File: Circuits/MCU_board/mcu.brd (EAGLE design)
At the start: 100 x 80 mm, 33 parts, among them U1 TCA9548APWR, U2 USBLC6-2P6, U3 LD39050PU33R, U4 LSM9DS1, U5 STM32L452RECT6

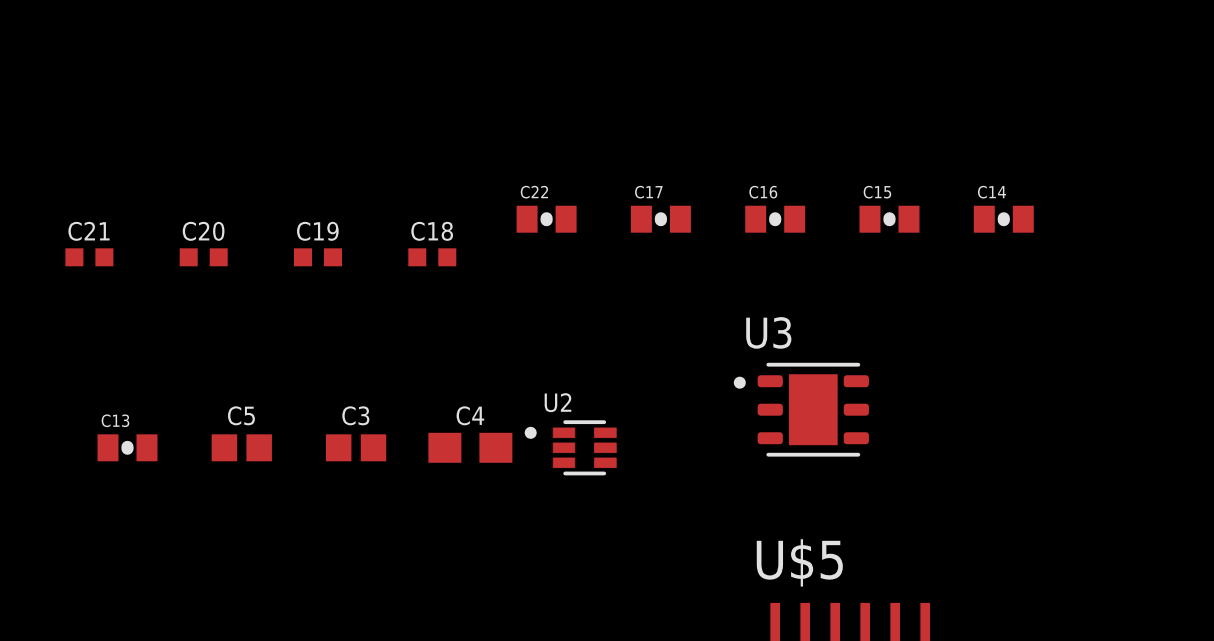
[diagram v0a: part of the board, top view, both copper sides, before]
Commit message: Delete caps
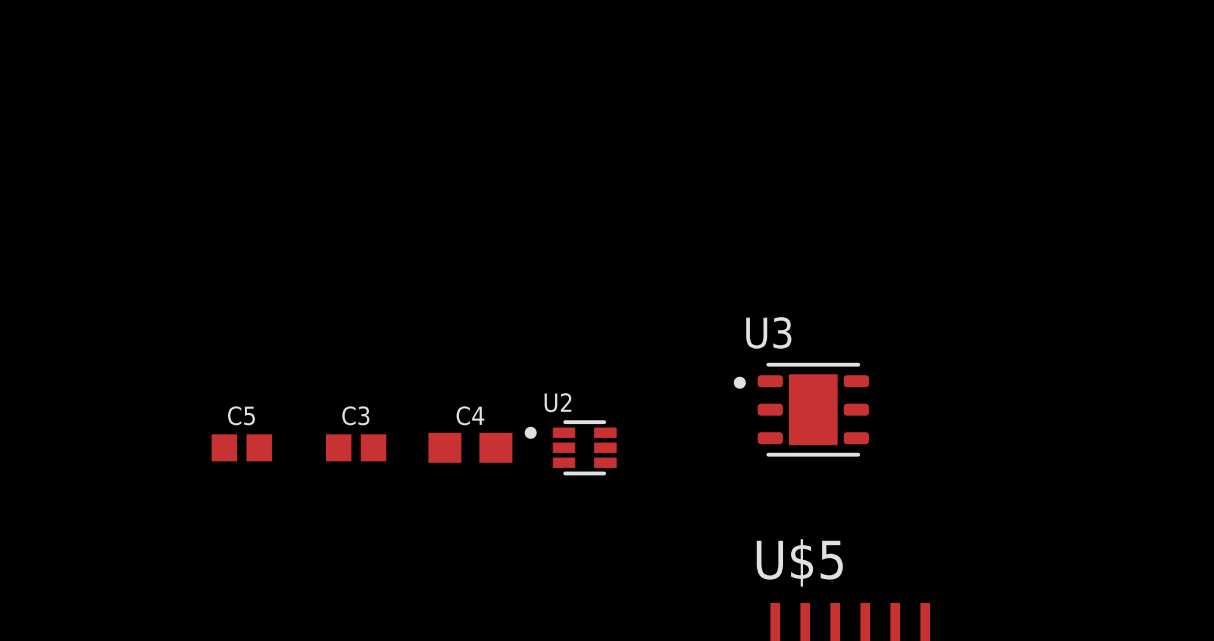
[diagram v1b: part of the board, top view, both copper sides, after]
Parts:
- removed C13, C14, C15, C16, C17, C22: 0.1uF, SparkFun-Retired:0402-CAP
- removed C18, C19, C20, C21: 2.2uF, SparkFun-Capacitors:0402-TIGHT
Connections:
- removed net N$21: C15.1, U5.48
- removed net N$22: C19.1, U5.47
- removed net N$26: C21.1, U5.18
- removed net N$29: C17.1, U5.64
- removed net N$30: C18.1, U5.63
- removed net N$31: C22.1, U5.31
- new net VDDA/VREF+: U5.13
- new net VDDUSB: U5.48
- new net VSS: U5.18, U5.31, U5.47, U5.63
- new net VSSA/VREF-: U5.12
- net GND: no longer C13.2, C14.2, C15.2, C16.2, C17.2, C18.2, C19.2, C20.2, C21.2, C22.2
- net VDD: now also U5.64; no longer C13.1, C14.1, C16.1, C20.1, U5.12, U5.13

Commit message: asdf
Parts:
- added C10, C12, C14, C16: 4.7uF, SparkFun-Capacitors:0603
- added C11, C13, C15, C9: 100nF, SparkFun-Capacitors:0603
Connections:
- removed net VDDUSB: U5.48
- removed net VSS: U5.18, U5.31, U5.47, U5.63
- net GND: now also C10.2, C11.2, C12.2, C13.2, C14.2, C15.2, C16.2, C9.2, U5.18, U5.31, U5.47, U5.63
- net VDD: now also C10.1, C11.1, C12.1, C13.1, C14.1, C15.1, C16.1, C9.1, U5.48
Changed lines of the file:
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@@
 <attribute name="VALUE" x="-44.45" y="-13.462" size="0.6096" layer="27" font="vector" ratio="20" align="top-center"/>
+</element>
+<element name="C9" library="SparkFun-Capacitors" package="0603" value="100nF" x="-44.45" y="-20.32" smashed="yes">
+<attribute name="NAME" x="-44.45" y="-19.558" size="0.6096" layer="25" font="vector" ratio="20" align="bottom-center"/>
+<attribute name="PROD_ID" value="CAP-12380" x="-44.45" y="-20.32" size="1.778" layer="27" display="off"/>
+<attribute name="VALUE" x="-44.45" y="-21.082" size="0.6096" layer="27" font="vector" ratio="20" align="top-center"/>
+</element>
+<element name="C10" library="SparkFun-Capacitors" package="0603" value="4.7uF" x="-44.45" y="-24.13" smashed="yes">
+<attribute name="NAME" x="-44.45" y="-23.368" size="0.6096" layer="25" font="vector" ratio="20" align="bottom-center"/>
+<attribute name="PROD_ID" value="CAP-12380" x="-44.45" y="-24.13" size="1.778" layer="27" display="off"/>
+<attribute name="VALUE" x="-44.45" y="-24.892" size="0.6096" layer="27" font="vector" ratio="20" align="top-center"/>
+</element>
+<element name="C11" library="SparkFun-Capacitors" package="0603" value="100nF" x="-44.45" y="-27.94" smashed="yes">
+<attribute name="NAME" x="-44.45" y="-27.178" size="0.6096" layer="25" font="vector" ratio="20" align="bottom-center"/>
+<attribute name="PROD_ID" value="CAP-12380" x="-44.45" y="-27.94" size="1.778" layer="27" display="off"/>
+<attribute name="VALUE" x="-44.45" y="-28.702" size="0.6096" layer="27" font="vector" ratio="20" align="top-center"/>
+</element>
+<element name="C12" library="SparkFun-Capacitors" package="0603" value="4.7uF" x="-44.45" y="-31.75" smashed="yes">
+<attribute name="NAME" x="-44.45" y="-30.988" size="0.6096" layer="25" font="vector" ratio="20" align="bottom-center"/>
+<attribute name="PROD_ID" value="CAP-12380" x="-44.45" y="-31.75" size="1.778" layer="27" display="off"/>
+<attribute name="VALUE" x="-44.45" y="-32.512" size="0.6096" layer="27" font="vector" ratio="20" align="top-center"/>
+</element>
+<element name="C13" library="SparkFun-Capacitors" package="0603" value="100nF" x="-44.45" y="-35.56" smashed="yes">
+<attribute name="NAME" x="-44.45" y="-34.798" size="0.6096" layer="25" font="vector" ratio="20" align="bottom-center"/>
+<attribute name="PROD_ID" value="CAP-12380" x="-44.45" y="-35.56" size="1.778" layer="27" display="off"/>
+<attribute name="VALUE" x="-44.45" y="-36.322" size="0.6096" layer="27" font="vector" ratio="20" align="top-center"/>
+</element>
+<element name="C14" library="SparkFun-Capacitors" package="0603" value="4.7uF" x="-44.45" y="-39.37" smashed="yes">
+<attribute name="NAME" x="-44.45" y="-38.608" size="0.6096" layer="25" font="vector" ratio="20" align="bottom-center"/>
+<attribute name="PROD_ID" value="CAP-12380" x="-44.45" y="-39.37" size="1.778" layer="27" display="off"/>
+<attribute name="VALUE" x="-44.45" y="-40.132" size="0.6096" layer="27" font="vector" ratio="20" align="top-center"/>
+</element>
+<element name="C15" library="SparkFun-Capacitors" package="0603" value="100nF" x="-44.45" y="-43.18" smashed="yes">
+<attribute name="NAME" x="-44.45" y="-42.418" size="0.6096" layer="25" font="vector" ratio="20" align="bottom-center"/>
+<attribute name="PROD_ID" value="CAP-12380" x="-44.45" y="-43.18" size="1.778" layer="27" display="off"/>
+<attribute name="VALUE" x="-44.45" y="-43.942" size="0.6096" layer="27" font="vector" ratio="20" align="top-center"/>
+</element>
+<element name="C16" library="SparkFun-Capacitors" package="0603" value="4.7uF" x="-44.45" y="-46.99" smashed="yes">
+<attribute name="NAME" x="-44.45" y="-46.228" size="0.6096" layer="25" font="vector" ratio="20" align="bottom-center"/>
+<attribute name="PROD_ID" value="CAP-12380" x="-44.45" y="-46.99" size="1.778" layer="27" display="off"/>
+<attribute name="VALUE" x="-44.45" y="-47.752" size="0.6096" layer="27" font="vector" ratio="20" align="top-center"/>
 </element>
 </elements>
@@
 <contactref element="U4" pad="20"/>
 <contactref element="U4" pad="19"/>
+<contactref element="C9" pad="2"/>
+<contactref element="C10" pad="2"/>
+<contactref element="C11" pad="2"/>
+<contactref element="C12" pad="2"/>
+<contactref element="C13" pad="2"/>
+<contactref element="C14" pad="2"/>
+<contactref element="C15" pad="2"/>
+<contactref element="C16" pad="2"/>
+<contactref element="U5" pad="63"/>
+<contactref element="U5" pad="47"/>
+<contactref element="U5" pad="31"/>
+<contactref element="U5" pad="18"/>
 <wire x1="32.635" y1="51.6922" x2="39.135" y2="51.6922" width="0" layer="19" extent="1-1"/>
 <wire x1="31.985" y1="51.6922" x2="32.635" y2="51.6922" width="0" layer="19" extent="1-1"/>
@@
 <wire x1="-20.86" y1="27.87" x2="-20.86" y2="36.76" width="0" layer="19" extent="1-1"/>
 <wire x1="-20.86" y1="18.98" x2="-20.86" y2="27.87" width="0" layer="19" extent="1-1"/>
-<wire x1="-34.83" y1="18.98" x2="-20.86" y2="18.98" width="0" layer="19" extent="1-1"/>
+<wire x1="-23.57" y1="13.37" x2="-20.86" y2="18.98" width="0" layer="19" extent="1-1"/>
+<wire x1="-31.42" y1="9.144" x2="-23.57" y2="13.37" width="0" layer="19" extent="1-1"/>
+<wire x1="-32.22" y1="9.144" x2="-31.42" y2="9.144" width="0" layer="19" extent="1-1"/>
+<wire x1="-14.57" y1="10.87" x2="-23.57" y2="13.37" width="0" layer="19" extent="1-1"/>
+<wire x1="-17.07" y1="1.87" x2="-14.57" y2="10.87" width="0" layer="19" extent="1-1"/>
+<wire x1="-23.57" y1="1.87" x2="-17.07" y2="1.87" width="0" layer="19" extent="1-1"/>
+<wire x1="-34.83" y1="18.98" x2="-32.22" y2="9.144" width="0" layer="19" extent="1-1"/>
 <wire x1="-34.83" y1="27.87" x2="-34.83" y2="18.98" width="0" layer="19" extent="1-1"/>
-<wire x1="-32.22" y1="9.144" x2="-34.83" y2="18.98" width="0" layer="19" extent="1-1"/>
-<wire x1="-31.42" y1="9.144" x2="-32.22" y2="9.144" width="0" layer="19" extent="1-1"/>
 <wire x1="-35.98" y1="-2.54" x2="-32.22" y2="9.144" width="0" layer="19" extent="1-1"/>
 <wire x1="-39.79" y1="-2.54" x2="-35.98" y2="-2.54" width="0" layer="19" extent="1-1"/>
@@
 <wire x1="-39.79" y1="-8.89" x2="-43.6" y2="-8.89" width="0" layer="19" extent="1-1"/>
 <wire x1="-35.98" y1="-8.89" x2="-39.79" y2="-8.89" width="0" layer="19" extent="1-1"/>
+<wire x1="-43.6" y1="-20.32" x2="-43.6" y2="-8.89" width="0" layer="19" extent="1-1"/>
+<wire x1="-43.6" y1="-24.13" x2="-43.6" y2="-20.32" width="0" layer="19" extent="1-1"/>
+<wire x1="-43.6" y1="-27.94" x2="-43.6" y2="-24.13" width="0" layer="19" extent="1-1"/>
+<wire x1="-43.6" y1="-31.75" x2="-43.6" y2="-27.94" width="0" layer="19" extent="1-1"/>
+<wire x1="-43.6" y1="-35.56" x2="-43.6" y2="-31.75" width="0" layer="19" extent="1-1"/>
+<wire x1="-43.6" y1="-39.37" x2="-43.6" y2="-35.56" width="0" layer="19" extent="1-1"/>
+<wire x1="-43.6" y1="-43.18" x2="-43.6" y2="-39.37" width="0" layer="19" extent="1-1"/>
+<wire x1="-43.6" y1="-46.99" x2="-43.6" y2="-43.18" width="0" layer="19" extent="1-1"/>
 </signal>
 <signal name="SWDIO">
@@
 <contactref element="U3" pad="4"/>
 <contactref element="C3" pad="1"/>
+<contactref element="C10" pad="1"/>
+<contactref element="C9" pad="1"/>
+<contactref element="C12" pad="1"/>
+<contactref element="C11" pad="1"/>
+<contactref element="C14" pad="1"/>
+<contactref element="C13" pad="1"/>
+<contactref element="C16" pad="1"/>
+<contactref element="C15" pad="1"/>
 <contactref element="U5" pad="64"/>
+<contactref element="U5" pad="48"/>
+<contactref element="U5" pad="32"/>
 <contactref element="U5" pad="19"/>
-<contactref element="U5" pad="32"/>
-<wire x1="-20.155" y1="43.5" x2="31.985" y2="57.5278" width="0" layer="19" extent="1-1"/>
+<wire x1="-45.3" y1="-43.18" x2="-45.3" y2="-46.99" width="0" layer="19" extent="1-1"/>
+<wire x1="-45.3" y1="-39.37" x2="-45.3" y2="-43.18" width="0" layer="19" extent="1-1"/>
+<wire x1="-45.3" y1="-35.56" x2="-45.3" y2="-39.37" width="0" layer="19" extent="1-1"/>
+<wire x1="-45.3" y1="-31.75" x2="-45.3" y2="-35.56" width="0" layer="19" extent="1-1"/>
+<wire x1="-45.3" y1="-27.94" x2="-45.3" y2="-31.75" width="0" layer="19" extent="1-1"/>
+<wire x1="-45.3" y1="-24.13" x2="-45.3" y2="-27.94" width="0" layer="19" extent="1-1"/>
+<wire x1="-45.3" y1="-20.32" x2="-45.3" y2="-24.13" width="0" layer="19" extent="1-1"/>
+<wire x1="-23.07" y1="1.87" x2="-45.3" y2="-20.32" width="0" layer="19" extent="1-1"/>
+<wire x1="-16.57" y1="1.87" x2="-23.07" y2="1.87" width="0" layer="19" extent="1-1"/>
+<wire x1="-14.57" y1="11.37" x2="-16.57" y2="1.87" width="0" layer="19" extent="1-1"/>
+<wire x1="-24.07" y1="13.37" x2="-14.57" y2="11.37" width="0" layer="19" extent="1-1"/>
+<wire x1="-20.155" y1="43.5" x2="-24.07" y2="13.37" width="0" layer="19" extent="1-1"/>
 <wire x1="-32.17" y1="43.18" x2="-20.155" y2="43.5" width="0" layer="19" extent="1-1"/>
 <wire x1="-37.41" y1="43.18" x2="-32.17" y2="43.18" width="0" layer="19" extent="1-1"/>
-<wire x1="-24.07" y1="13.37" x2="-20.155" y2="43.5" width="0" layer="19" extent="1-1"/>
-<wire x1="-23.07" y1="1.87" x2="-24.07" y2="13.37" width="0" layer="19" extent="1-1"/>
-<wire x1="-16.57" y1="1.87" x2="-23.07" y2="1.87" width="0" layer="19" extent="1-1"/>
+<wire x1="31.985" y1="57.5278" x2="-20.155" y2="43.5" width="0" layer="19" extent="1-1"/>
 </signal>
 <signal name="USB_D-">
@@
 <wire x1="-45.925" y1="-4.455" x2="-45.3" y2="-12.7" width="0" layer="19" extent="1-1"/>
 </signal>
-<signal name="VSS">
-<contactref element="U5" pad="63"/>
-<contactref element="U5" pad="18"/>
-<contactref element="U5" pad="31"/>
-<contactref element="U5" pad="47"/>
-<wire x1="-17.07" y1="1.87" x2="-23.57" y2="1.87" width="0" layer="19" extent="1-1"/>
-<wire x1="-14.57" y1="10.87" x2="-17.07" y2="1.87" width="0" layer="19" extent="1-1"/>
-<wire x1="-23.57" y1="13.37" x2="-14.57" y2="10.87" width="0" layer="19" extent="1-1"/>
-</signal>
 <signal name="VSSA/VREF-">
 <contactref element="U5" pad="12"/>
@@
 <contactref element="U5" pad="13"/>
 </signal>
-<signal name="VDDUSB">
-<contactref element="U5" pad="48"/>
-</signal>
 </signals>

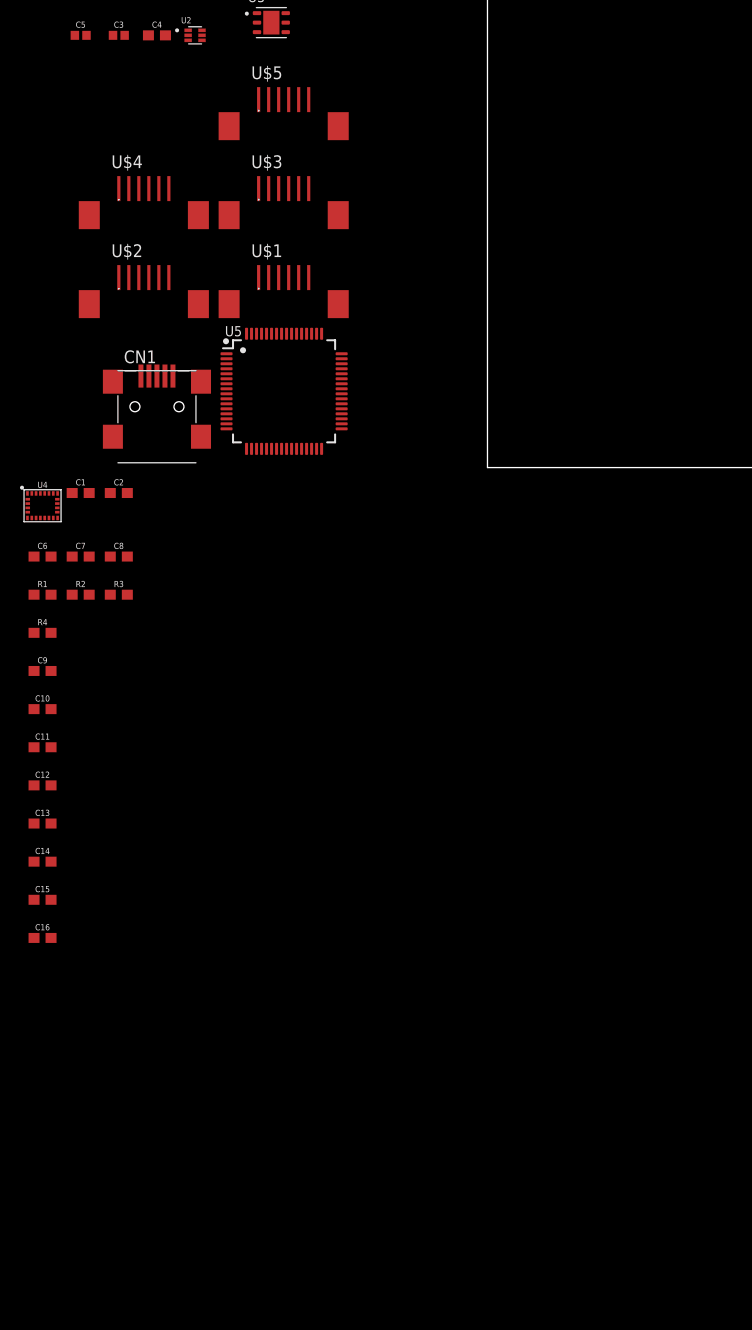
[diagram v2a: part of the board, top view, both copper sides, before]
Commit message: Add connectors on mcu board
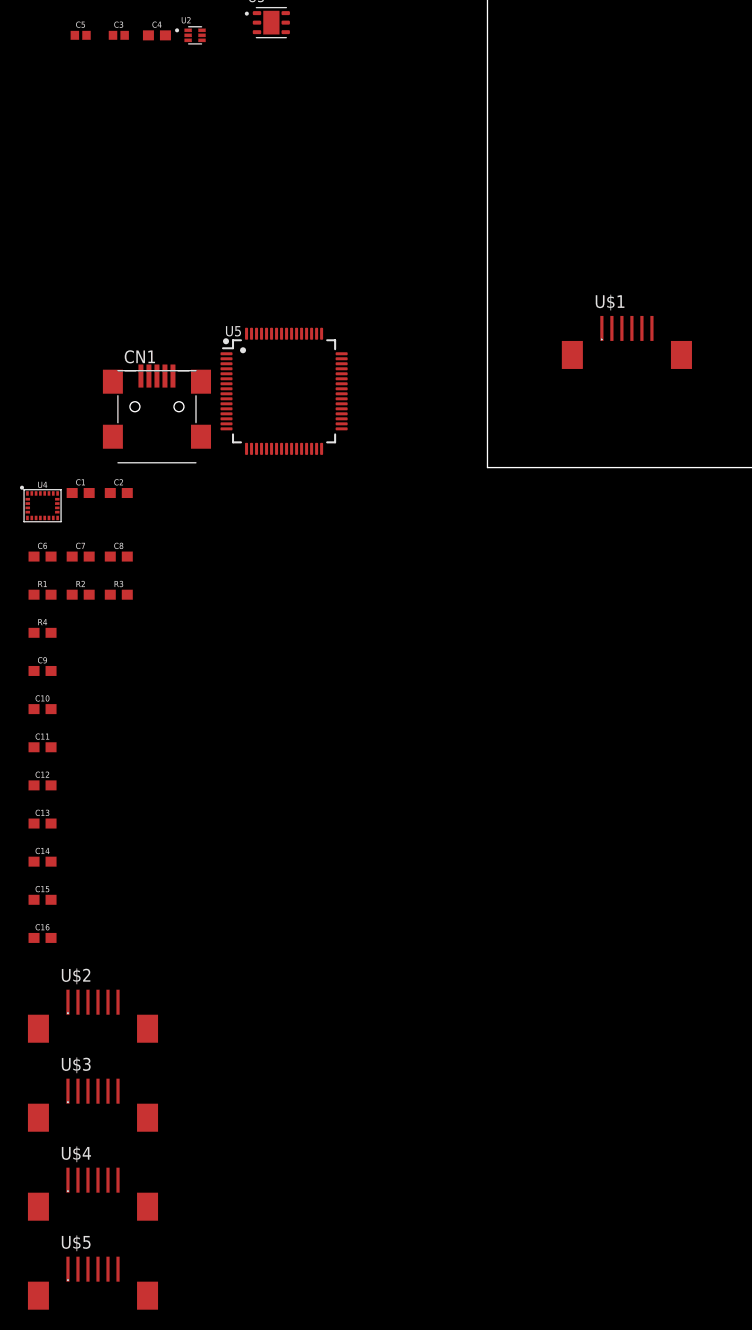
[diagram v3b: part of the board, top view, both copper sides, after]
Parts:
- moved U$5 118.4 mm to (-41.9, -81.3)
- moved U$4 99.2 mm to (-41.9, -72.4)
- moved U$3 92.2 mm to (-41.9, -63.5)
- moved U$2 72.6 mm to (-41.9, -54.6)
- moved U$1 34.7 mm to (11.4, 12.7)
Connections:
- net SCL5: now also U$5.5
- net SCL7: no longer U$5.5
- net SDA5: now also U$5.6
- net SDA7: no longer U$5.6
- net VCC: no longer U$1.4, U$2.4, U$3.4, U$4.4, U$5.4
- net VDD: now also U$1.4, U$2.4, U$3.4, U$4.4, U$5.4

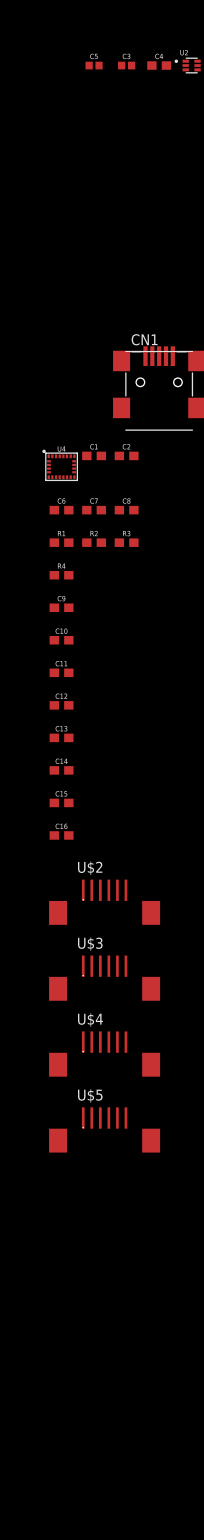
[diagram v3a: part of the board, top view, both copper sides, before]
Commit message: Add SWD and reset to MCU board
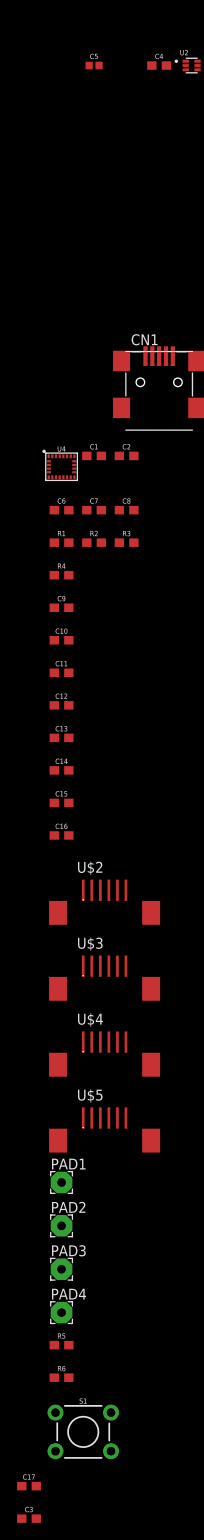
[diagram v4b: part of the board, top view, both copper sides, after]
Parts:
- added C17: 100nF, SparkFun-Capacitors:0603
- added PAD1, PAD2, PAD3, PAD4: WIREPAD2,54/1,0, wirepad:2,54/1,0
- added R5, R6: 10k, SparkFun-Resistors:0603
- added S1: MOMENTARY-SWITCH-SPST-PTH-6.0MM, SparkFun-Switches:TACTILE_SWITCH_PTH_6.0MM
- C3: value 1.0uF -> 1 uF; device SparkFun-Capacitors:0402 -> SparkFun-Capacitors:0603
- moved C3 170.6 mm to (-48.3, -127.0)
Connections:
- new net N$4: C17.1, S1.3, U5.7
- net GND: now also C17.2, PAD4.1, R5.1, S1.1
- net SWCLK: now also PAD2.1, R5.2
- net SWDIO: now also PAD1.1, R6.1
- net VCC: now also R6.2
- net VDD: now also PAD3.1

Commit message: Add I2C mux reset GPIO
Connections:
- new net I2C_MUX_RST: U1.3, U5.22
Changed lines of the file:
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@@
 <wire x1="-26.07" y1="8.37" x2="-45.1612" y2="-119.1006" width="0" layer="19" extent="1-1"/>
+</signal>
+<signal name="I2C_MUX_RST">
+<contactref element="U5" pad="22"/>
+<contactref element="U1" pad="3"/>
+<wire x1="-21.57" y1="1.87" x2="33.285" y2="51.6922" width="0" layer="19" extent="1-1"/>
 </signal>
 </signals>

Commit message: set I2C lines for IMU on mcu board
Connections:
- net SCL6: now also U4.2
- net SCL7: no longer U4.2
- net SDA6: now also U4.4
- net SDA7: no longer U4.4
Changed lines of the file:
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@@
 <signal name="SCL7">
 <contactref element="U1" pad="20"/>
-<contactref element="U4" pad="2"/>
-<wire x1="-45.925" y1="-3.165" x2="34.585" y2="57.5278" width="0" layer="19" extent="1-1"/>
 </signal>
 <signal name="SDA7">
 <contactref element="U1" pad="19"/>
-<contactref element="U4" pad="4"/>
-<wire x1="-45.925" y1="-4.025" x2="35.235" y2="57.5278" width="0" layer="19" extent="1-1"/>
 </signal>
 <signal name="SCL6">
 <contactref element="U1" pad="18"/>
 <contactref element="U$5" pad="1"/>
-<wire x1="35.885" y1="57.5278" x2="-41.91" y2="-80.08" width="0" layer="19" extent="1-1"/>
+<contactref element="U4" pad="2"/>
+<wire x1="-45.925" y1="-3.165" x2="-41.91" y2="-80.08" width="0" layer="19" extent="1-1"/>
+<wire x1="35.885" y1="57.5278" x2="-45.925" y2="-3.165" width="0" layer="19" extent="1-1"/>
 </signal>
 <signal name="SDA6">
 <contactref element="U1" pad="17"/>
 <contactref element="U$5" pad="2"/>
-<wire x1="36.535" y1="57.5278" x2="-40.91" y2="-80.08" width="0" layer="19" extent="1-1"/>
+<contactref element="U4" pad="4"/>
+<wire x1="-45.925" y1="-4.025" x2="-40.91" y2="-80.08" width="0" layer="19" extent="1-1"/>
+<wire x1="36.535" y1="57.5278" x2="-45.925" y2="-4.025" width="0" layer="19" extent="1-1"/>
 </signal>
 <signal name="SCL5">
